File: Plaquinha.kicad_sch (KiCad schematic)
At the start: 35 parts, among them J1 Screw_Terminal_01x02, J10 Conn_01x15_Socket, J11 Conn_01x15_Socket, J12 Conn_01x06_Socket, J13 Conn_01x06_Socket, J2 Conn_01x10_Socket, J3 Conn_01x10_Socket, J4 Conn_01x06_Socket, J5 Conn_01x04_Socket, J6 Conn_01x04_Socket, J7 Conn_01x06_Socket, J8 Conn_01x03_Socket, J9 Conn_01x03_Socket, U1 L7805, U10 TA6586, U3 TA6586, U5 L7805, U9 ESP32-DEVKIT-V1

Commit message: PCB e Sketch atualizados
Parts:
- removed C10: 680µF, Capacitor_THT:CP_Radial_D12.5mm_P5.00mm, symbol Device:C
- J13, J7: footprint (none) -> Connector_PinHeader_2.54mm:PinHeader_1x06_P2.54mm_Vertical
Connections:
- net D21 is gone; now on net SDA: J10.11 (Pin_11)
- net D22 is gone; now on net SCL: J10.14 (Pin_14)
- net D25 is gone; now on net ECHO: J11.8 (Pin_8)
- net D26 is gone; now on net TRIG: J11.7 (Pin_7)
- net ECHO: now also U9.23 (D25); no longer U9.6 (RX2)
- net TRIG: now also U9.24 (D26); no longer U9.7 (TX2)
- net RX2: no longer names the net of J10.6 (Pin_6)
- net TX2: no longer names the net of J10.7 (Pin_7)

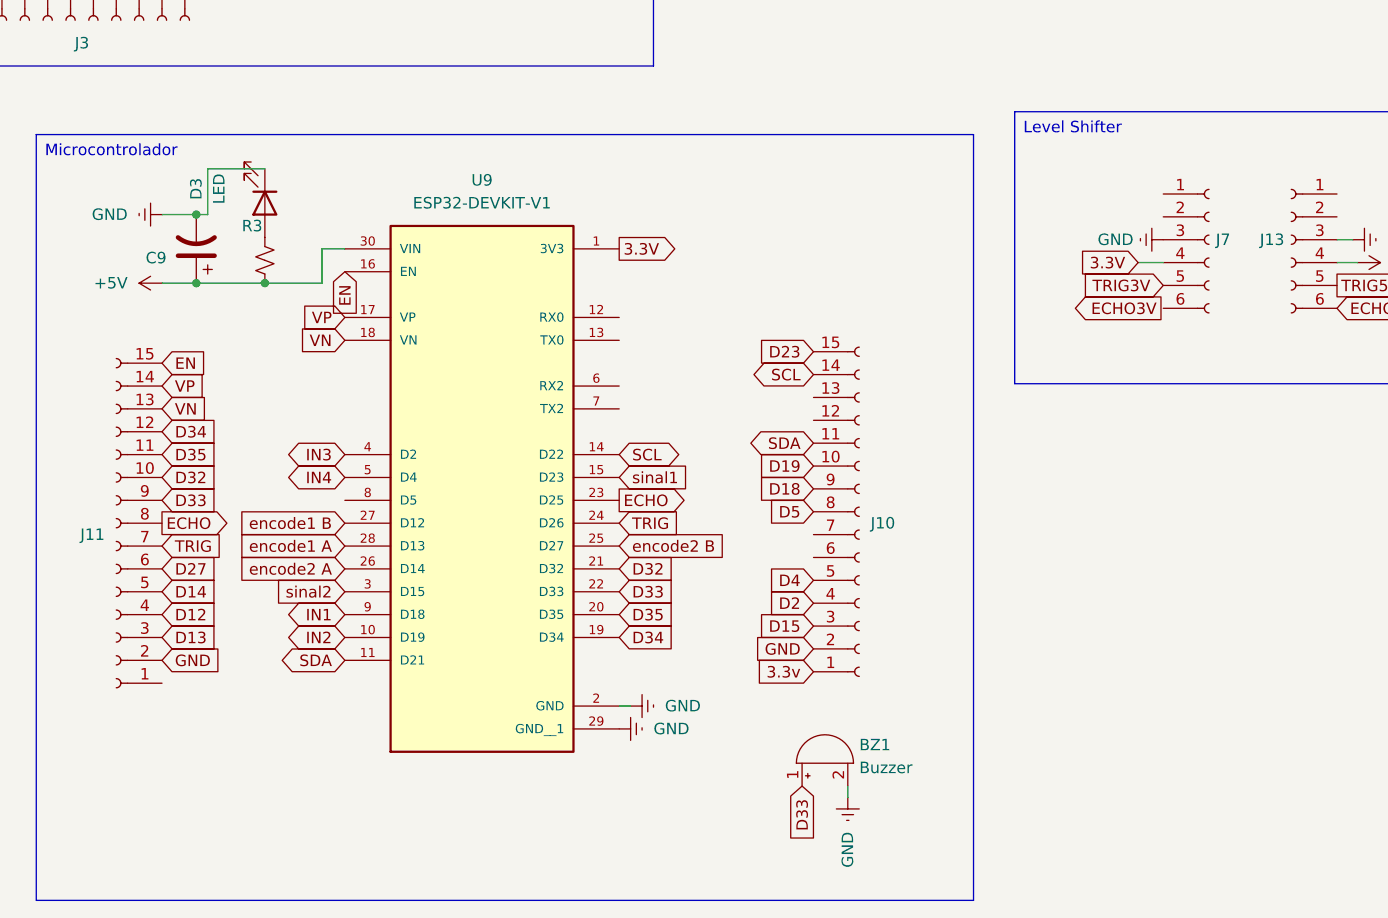
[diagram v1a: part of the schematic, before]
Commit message: PCI finalizada e shunt jumper adicionado ao sketch
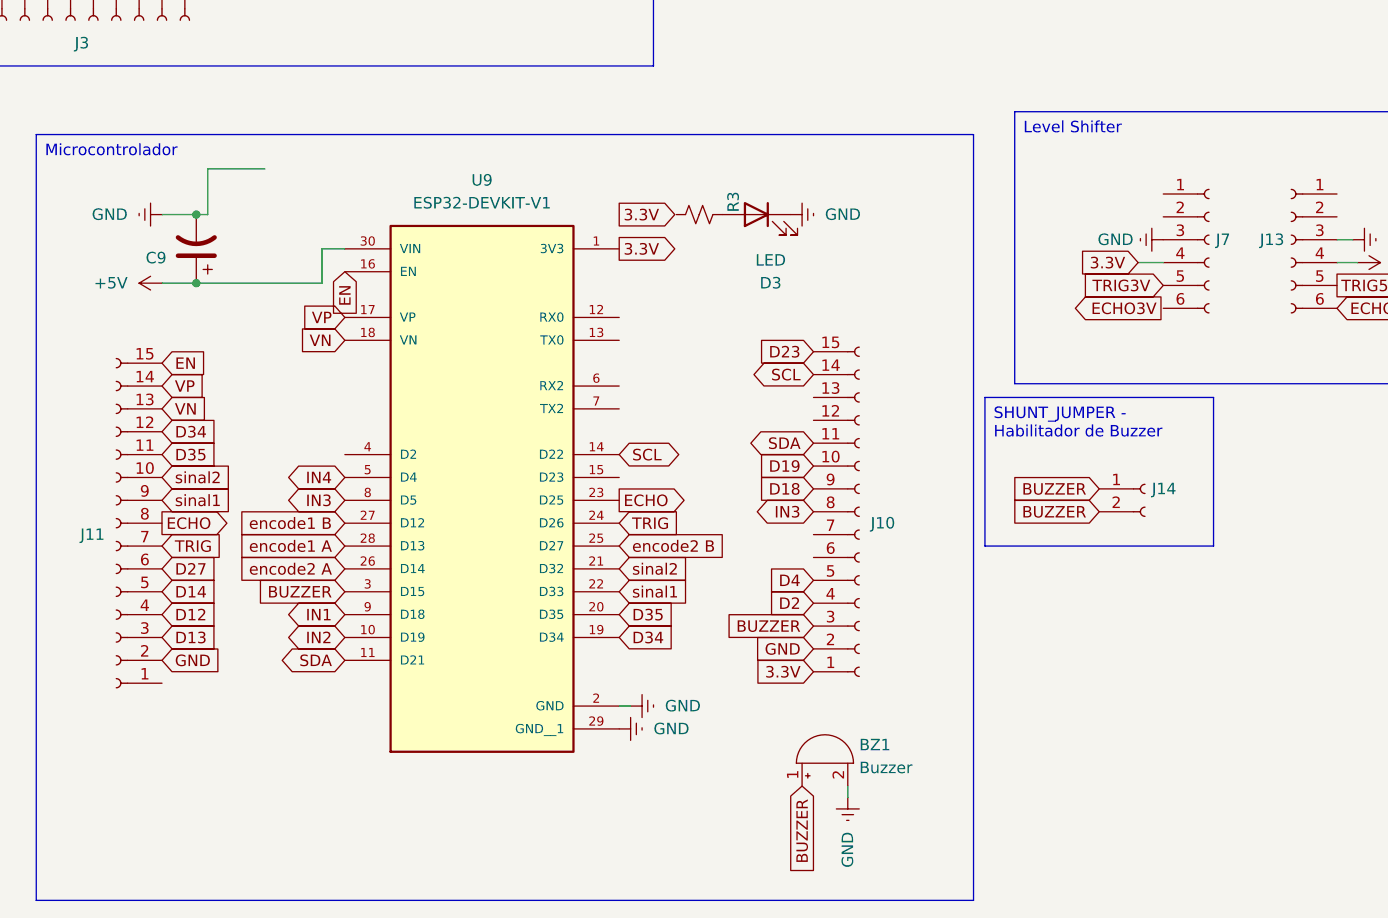
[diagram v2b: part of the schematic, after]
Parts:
- added J14: Conn_01x06_Socket, Connector_PinHeader_2.54mm:PinHeader_1x02_P2.54mm_Vertical, symbol Connector:Conn_01x02_Socket
- C1: footprint Capacitor_THT:C_Disc_D5.0mm_W2.5mm_P2.50mm -> Capacitor_THT:C_Disc_D5.0mm_W2.5mm_P5.00mm
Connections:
- net 3.3v is gone; now on net 3.3V: J10.1 (Pin_1)
- net D32 is gone; now on net sinal2: J11.10 (Pin_10), U9.21 (D32)
- net D5 is gone; now on net IN3: J10.8 (Pin_8)
- net +5V: no longer R3.1
- net IN3: now also U9.8 (D5); no longer U9.4 (D2)
- net sinal1: now also J11.9 (Pin_9), U9.22 (D33); no longer U9.15 (D23)
- net sinal2: no longer U9.3 (D15)
- net D15 renamed BUZZER
- net BUZZER: now also BZ1.1 (+), U9.3 (D15), J14.1 (Pin_1), J14.2 (Pin_2)
- removed net D33: BZ1.1 (+), J11.9 (Pin_9), U9.22 (D33)
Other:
- moved on the sheet: D3, R3

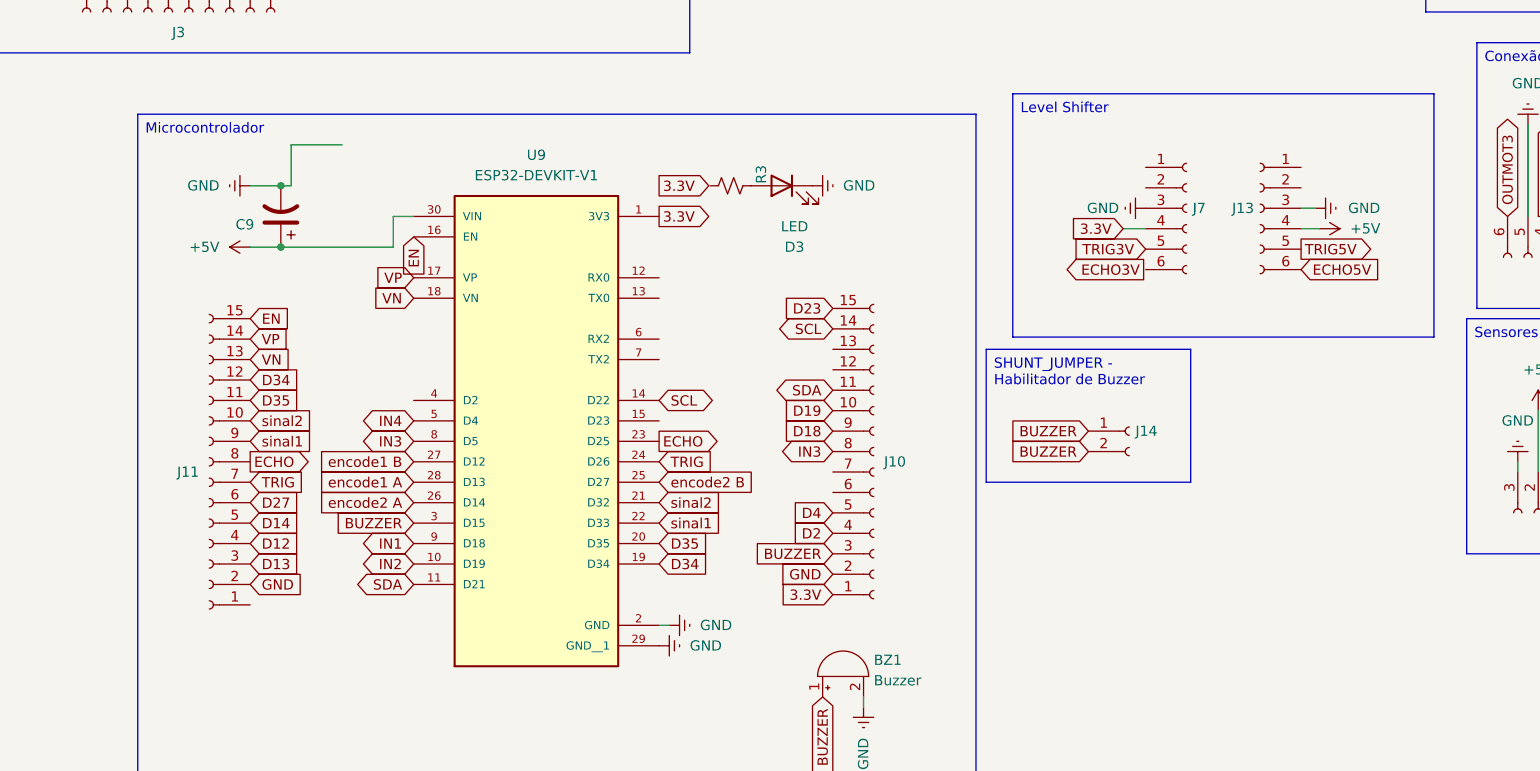
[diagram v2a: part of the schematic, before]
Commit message: Atualizei PCI, tirei jumpers desnecessários e simplifiquei trilhas
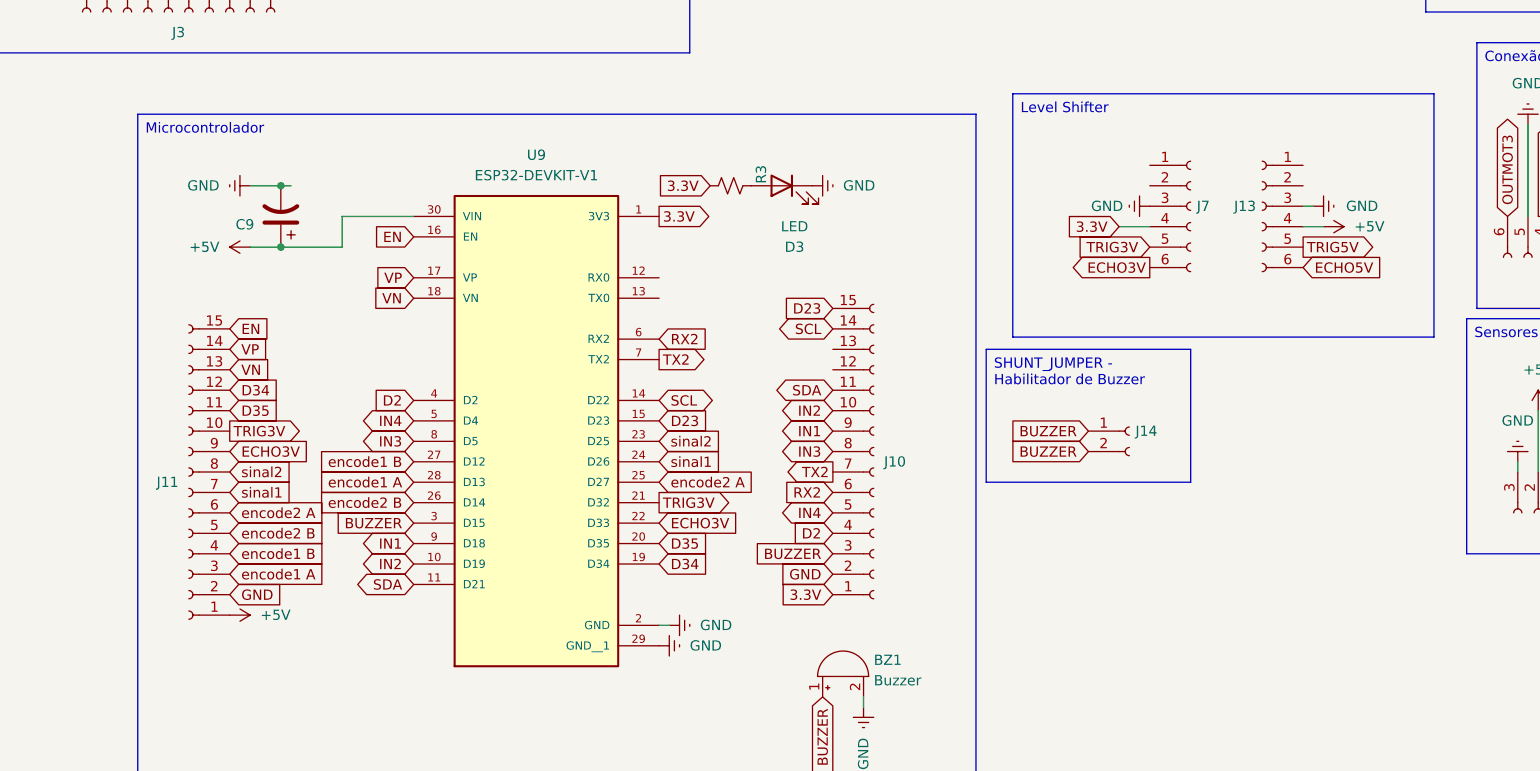
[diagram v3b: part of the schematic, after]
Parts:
- C9: footprint Capacitor_THT:CP_Radial_D8.0mm_P3.50mm -> Capacitor_THT:CP_Radial_D8.0mm_P5.00mm
- J5: footprint Connector_PinHeader_2.54mm:PinHeader_1x04_P2.54mm_Vertical -> Connector_JST:JST_EH_B4B-EH-A_1x04_P2.50mm_Vertical
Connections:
- net D12 is gone; now on net encode1 B: J11.4 (Pin_4)
- net D13 is gone; now on net encode1 A: J11.3 (Pin_3)
- net D14 is gone; now on net encode2 B: J11.5 (Pin_5)
- net D18 is gone; now on net IN1: J10.9 (Pin_9)
- net D19 is gone; now on net IN2: J10.10 (Pin_10)
- net D27 is gone; now on net encode2 A: J11.6 (Pin_6)
- net D4 is gone; now on net IN4: J10.5 (Pin_5)
- net ECHO is gone; now on net sinal2: J11.8 (Pin_8), U9.23 (D25)
- net TRIG is gone; now on net sinal1: J11.7 (Pin_7), U9.24 (D26)
- net +5V: now also J11.1 (Pin_1)
- net 3.3V: now also R3.1
- net D2: now also U9.4 (D2)
- net D23: now also U9.15 (D23)
- net ECHO3V: now also J11.9 (Pin_9), J7.6 (Pin_6), U9.22 (D33)
- net TRIG3V: now also J11.10 (Pin_10), U9.21 (D32)
- net encode2 A: now also U9.25 (D27); no longer U9.26 (D14)
- net encode2 B: now also U9.26 (D14); no longer U9.25 (D27)
- net sinal1: no longer J11.9 (Pin_9), U9.22 (D33)
- net sinal2: no longer J11.10 (Pin_10), U9.21 (D32)
- net RX2: now reaches J10.6 (Pin_6)
- net RX2: now also U9.6 (RX2)
- net TX2: now reaches J10.7 (Pin_7)
- net TX2: now also U9.7 (TX2)
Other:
- moved on the sheet: J11, J7

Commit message: Placa corrigida e pronta para impressão
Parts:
- added J15, J16: Conn_01x06_Socket, Connector_PinHeader_2.54mm:PinHeader_1x06_P2.54mm_Vertical, symbol Connector:Conn_01x06_Socket
- C2, C3: value 100µF -> 470µF
- C9: value 100µF -> 470µF; footprint Capacitor_THT:CP_Radial_D8.0mm_P5.00mm -> Capacitor_THT:CP_Radial_D8.0mm_P3.50mm
- J12, J4: value Conn_01x06_Socket -> Conn_01x06_Socket JST
- J14: value Conn_01x06_Socket -> Conn_01x02_Socket
- R3: value R_Small_US -> 470R
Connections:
- net +5V: now also J16.3 (Pin_3)
- net 3.3V: now also J15.4 (Pin_4); no longer R3.1
- net ECHO3V: now also J15.6 (Pin_6)
- net ECHO5V: now also J16.1 (Pin_1)
- net GND: now also J15.3 (Pin_3), J16.4 (Pin_4)
- net TRIG3V: now also J15.5 (Pin_5)
- net TRIG5V: now also J16.2 (Pin_2)
- net at C7.1, D1.1 (K), U1.1 (IN)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: now also R3.1
- net at J7.1 (Pin_1): now also J15.1 (Pin_1)
- net at J7.2 (Pin_2): now also J15.2 (Pin_2)
- net at J13.1 (Pin_1): now also J16.6 (Pin_6)
- net at J13.2 (Pin_2): now also J16.5 (Pin_5)
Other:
- moved on the sheet: D3, J13, J7, R3
